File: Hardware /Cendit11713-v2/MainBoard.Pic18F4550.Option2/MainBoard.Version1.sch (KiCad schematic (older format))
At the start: 62 parts, among them CON1 POWER_BUS, CON2 ICSP_CON, CON3 USB_CON, J1 RESET_CON, J2 PIN_HEADER_20P, J3 PIN_HEADER_20P, J4 SATA_PLUG _22P_SMT, J5 SATA_PLUG _22P_SMT, Q1 2N2222, U1 PIC18F4550-I/P, U2 MPL3115A2, U3 PCF85263A, Y1 Crystal, Y2 32.768KHZ

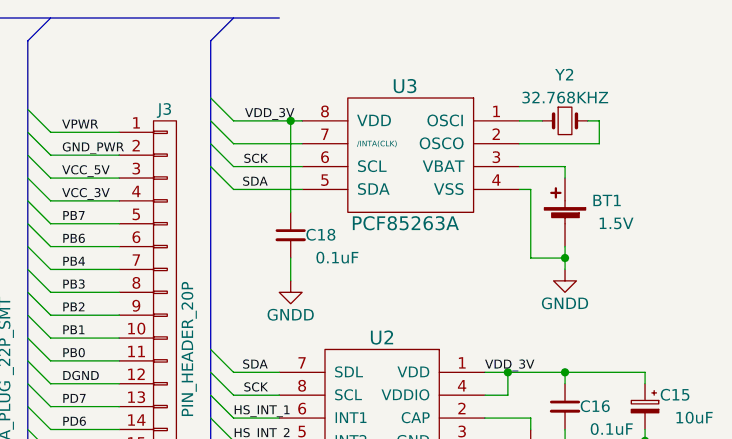
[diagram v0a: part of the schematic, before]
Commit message: En CenditLab + Cendit11713
  - Edicion de PCB tarjeta madre
  - Revision de PCB expansor Viking
  - Archivos gerber generados

  - Edicion de clases UI
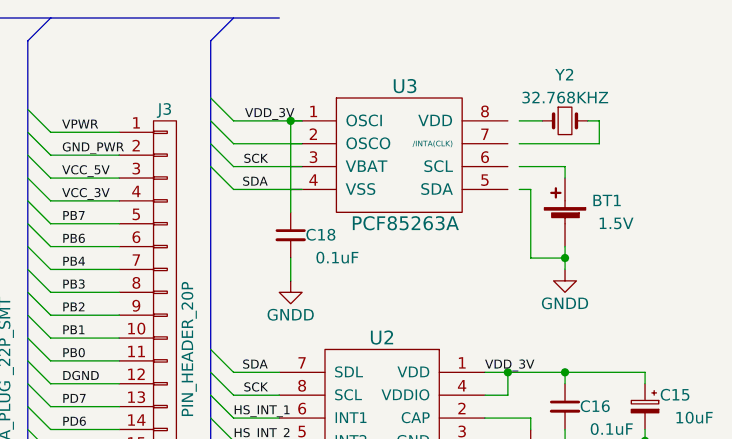
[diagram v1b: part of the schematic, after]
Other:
- moved on the sheet: U3
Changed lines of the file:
@@
 EESchema Schematic File Version 2
-LIBS:MainBoard-rescue
 LIBS:adc-dac
 LIBS:memory
@@
 LIBS:74xx
 LIBS:cmos4000
+LIBS:eSim_Analog
+LIBS:eSim_Devices
+LIBS:eSim_Digital
+LIBS:eSim_Hybrid
+LIBS:eSim_Miscellaneous
+LIBS:eSim_Power
+LIBS:eSim_Sources
+LIBS:eSim_Subckt
+LIBS:eSim_User
+LIBS:eSim_Plot
+LIBS:eSim_PSpice
 LIBS:CenditBasic
-LIBS:MainBoard-cache
 EELAYER 25 0
 EELAYER END
@@
 L PCF85263A U3
 U 1 1 5A027CF7
-P 9700 1250
-F 0 "U3" H 9850 1650 60  0000 C CNN
-F 1 "PCF85263A" H 9850 1050 60  0000 C CNN
-F 2 "CenditFootprints:PCF85263A_SO8" H 9700 1250 60  0001 C CNN
-F 3 "" H 9700 1250 60  0001 C CNN
-	1    9700 1250
-	-1   0    0    -1
-$EndComp
-$Comp
+P 9400 1250
+F 0 "U3" H 9550 1650 60  0000 C CNN
+F 1 "PCF85263A" H 9550 1050 60  0000 C CNN
+F 2 "CenditFootprints:PCF85263A_SO8" H 9400 1250 60  0001 C CNN
+F 3 "" H 9400 1250 60  0001 C CNN
+	1    9400 1250
+	1    0    0    -1
+$EndComp
+$Comp

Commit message: En Cendit11713 + CenditLab respaldo
  - Se revisan tarjetas
  - Correccion en PCB GPIB
  - Se inicia tarjeta madre en una pieza (MainBoard.OnePiece)
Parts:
- CON1: symbol POWER_BUS -> POWER_BUS-RESCUE-MainBoard.Version1
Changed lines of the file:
@@
 EESchema Schematic File Version 2
+LIBS:MainBoard.Version1-rescue
 LIBS:adc-dac
 LIBS:memory
@@
 LIBS:eSim_PSpice
 LIBS:CenditBasic
+LIBS:MainBoard.Version1-cache
 EELAYER 25 0
 EELAYER END
@@
 	1650 6800 1500 6800
 $Comp
-L POWER_BUS CON1
+L POWER_BUS-RESCUE-MainBoard.Version1 CON1
 U 1 1 5A0A188A
 P 700 1950
